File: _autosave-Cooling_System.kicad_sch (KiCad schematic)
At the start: 12 parts, among them J1 BAT_IN, J2 FAN_OUT, Q1 Q_PMOS_GSD, Q2 Q_NMOS_GDS, U1 Buck_Module

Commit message: Added some more stuff. Teensy in
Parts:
- added C3: 100 microF, symbol Device:C_Small
- added U2: Teensy4.1, symbol teensy:Teensy4.1
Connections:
- net +12V_FAN: now also Q1.3 (VPROT), U1.1 (Pin_1); no longer F1.2, Q1.2 (S), R2.1
- net GND: now also C3.2, U2.47 (GND)
- net PWM_CNTRL: now also U2.3 (1_TX1_CTX2_MISO1)
- net at D2.1 (K): now also J2.+12V_FAN (Pin_1), C3.1
- net at D2.2 (A): now also J2.FAN_NEG (Pin_2), Q2.2 (D)
- new net: F1.2, Q1.2 (S), R2.1
- new net 3V3: U2.51 (3V3)
- new net TEMP1_ADC: U2.36 (14_A0_TX3_SPDIF_OUT)
- new net VOUT +5V: U2.48 (VIN)
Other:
- moved on the sheet: D2

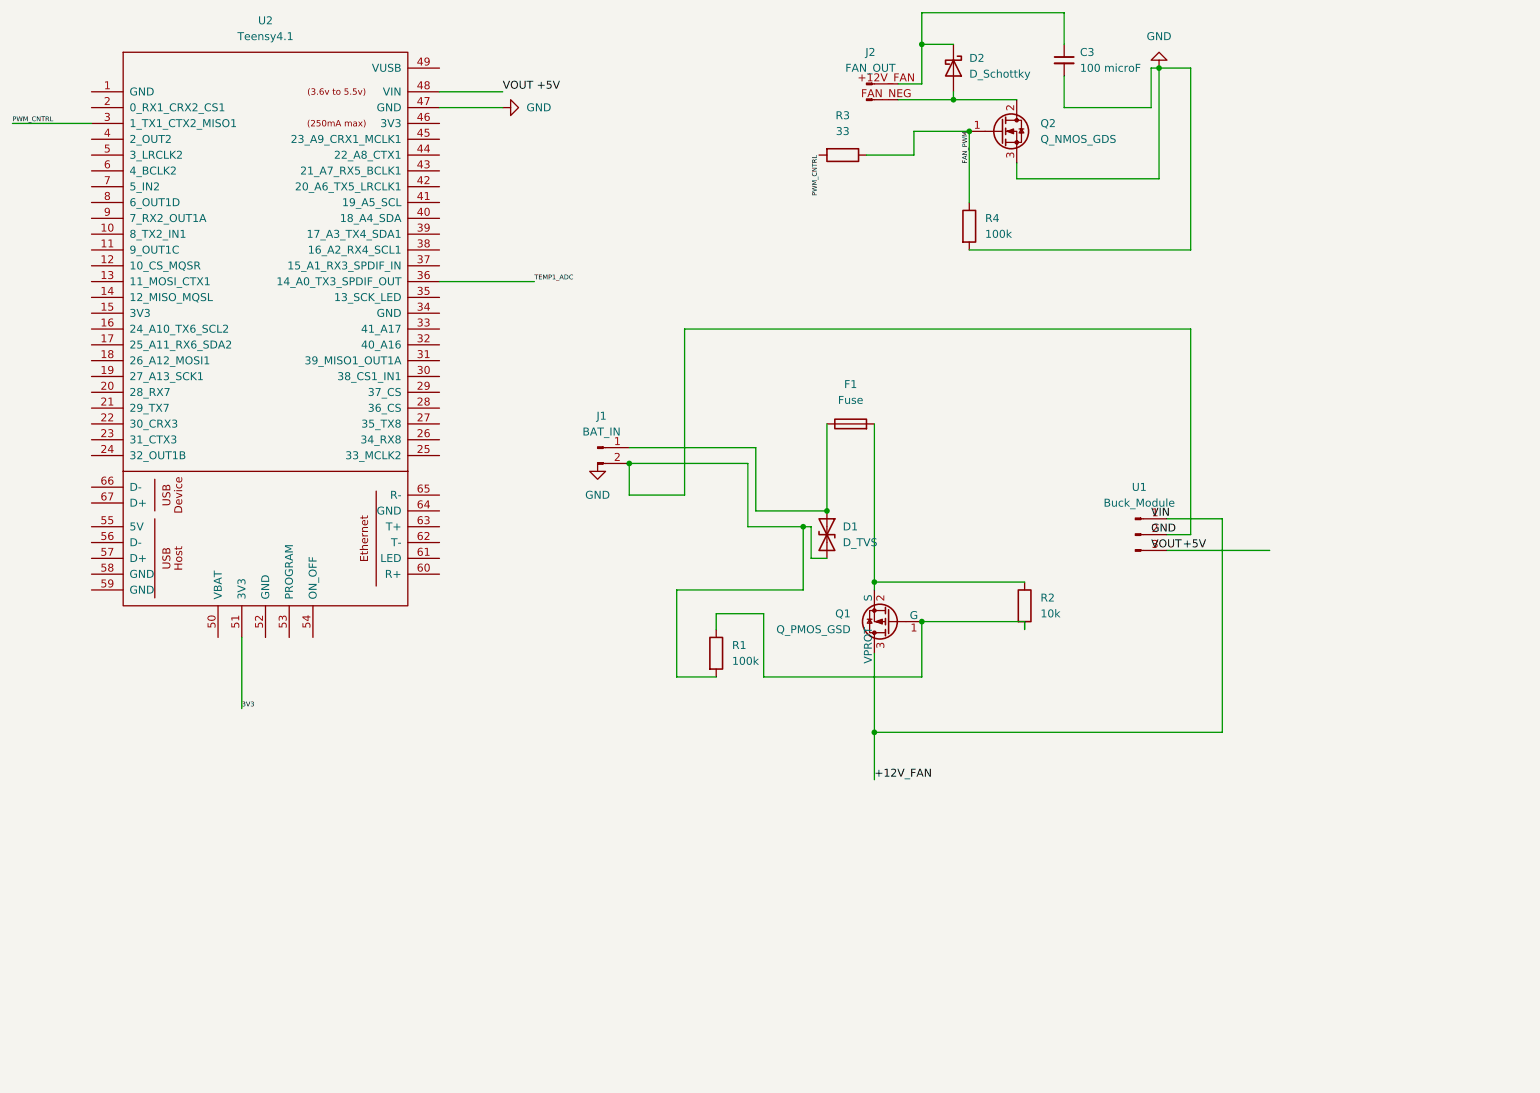
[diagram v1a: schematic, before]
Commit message: circuit schematic with metric logging output
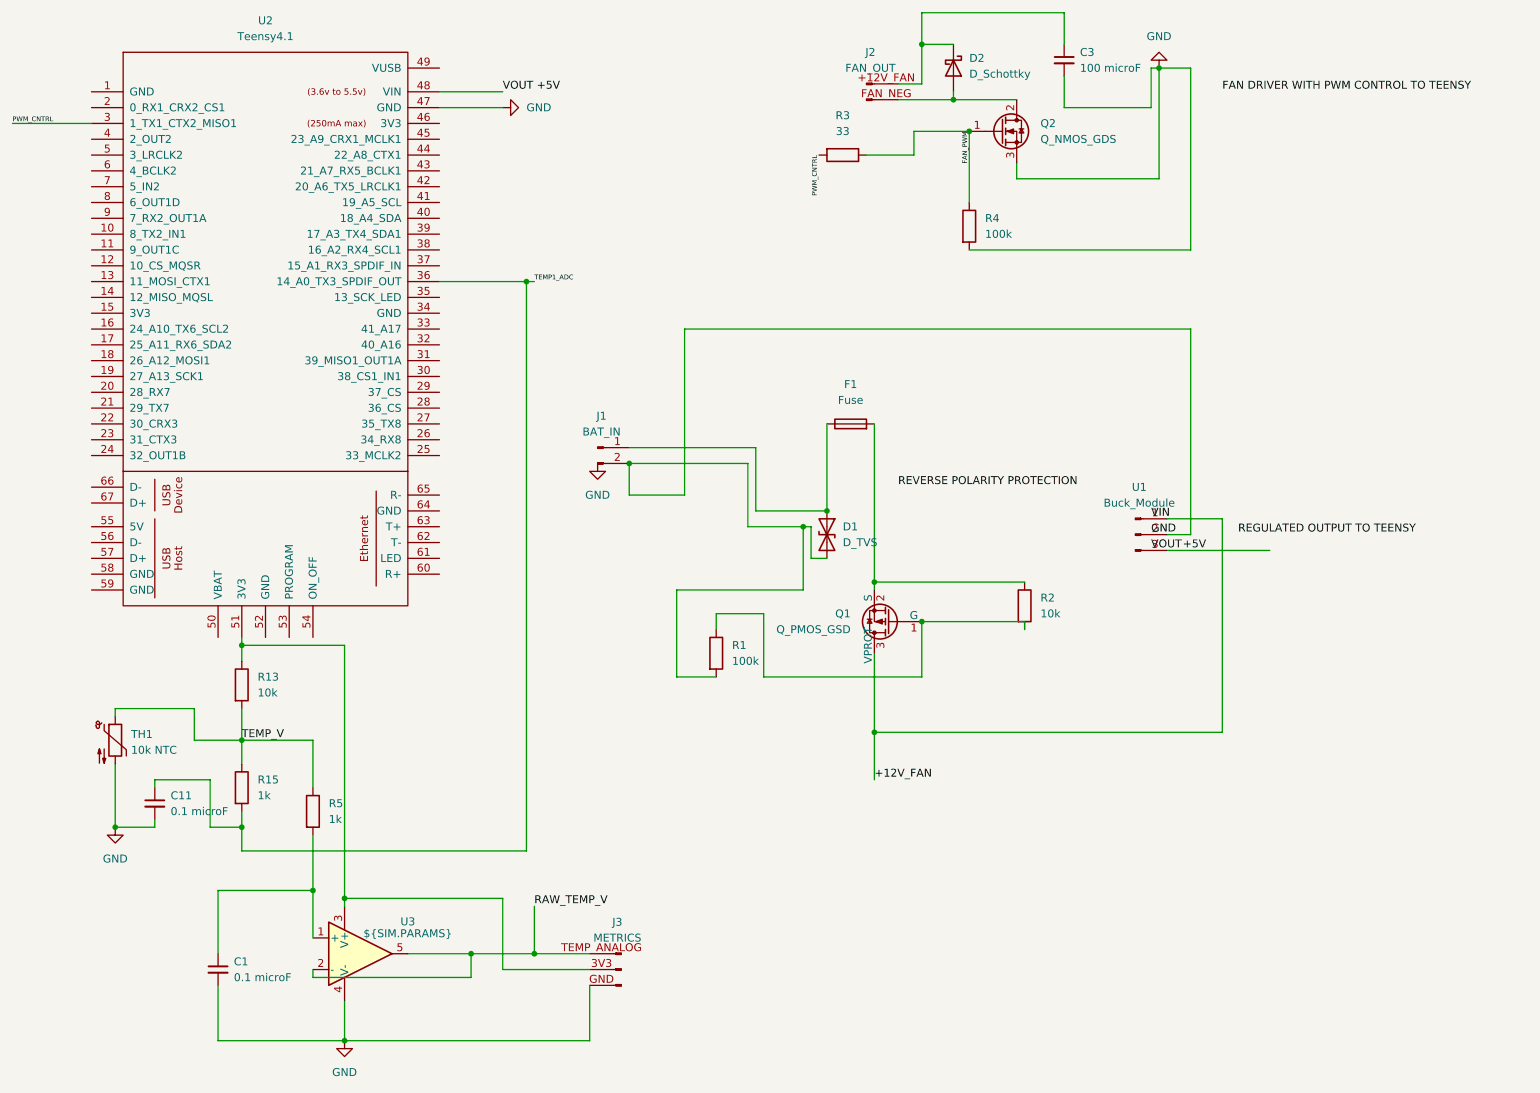
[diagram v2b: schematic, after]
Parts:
- added C1, C11: 0.1 microF, symbol Device:C_Small
- added J3: METRICS, symbol Connector:Conn_01x03_Pin
- added R13: 10k, symbol Device:R
- added R15, R5: 1k, symbol Device:R
- added TH1: 10k NTC, symbol Device:Thermistor_NTC
- added U3: ${SIM.PARAMS}, symbol Simulation_SPICE:OPAMP
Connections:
- net GND: now also C1.2, C11.2, J3.GND (Pin_3), TH1.2, U3.4 (V-)
- net TEMP1_ADC: now also C11.1, R15.2
- net 3V3: no longer names the net of U2.51 (3V3)
- net 3V3: now also J3.3V3 (Pin_2), R13.1, U3.3 (V+)
- new net: C1.1, R5.2, U3.1 (+)
- new net RAW_TEMP_V: J3.TEMP_ANALOG (Pin_1), U3.2 (-), U3.5
- new net TEMP_V: R13.2, R15.1, R5.1, TH1.1
